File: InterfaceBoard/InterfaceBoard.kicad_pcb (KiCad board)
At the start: 2 copper layers, 100 x 85 mm, 115 parts, among them J1 Conn_ARM_JTAG_SWD_10, J2 USB_B, J3 Keithley_50-Pin_Connector, P1 RB1-125BAG1A, Q1 BC848W, Q2 BC848W, Q3 BC848W, U1 W5500, U2 FT231XS, Y1 25 MHz

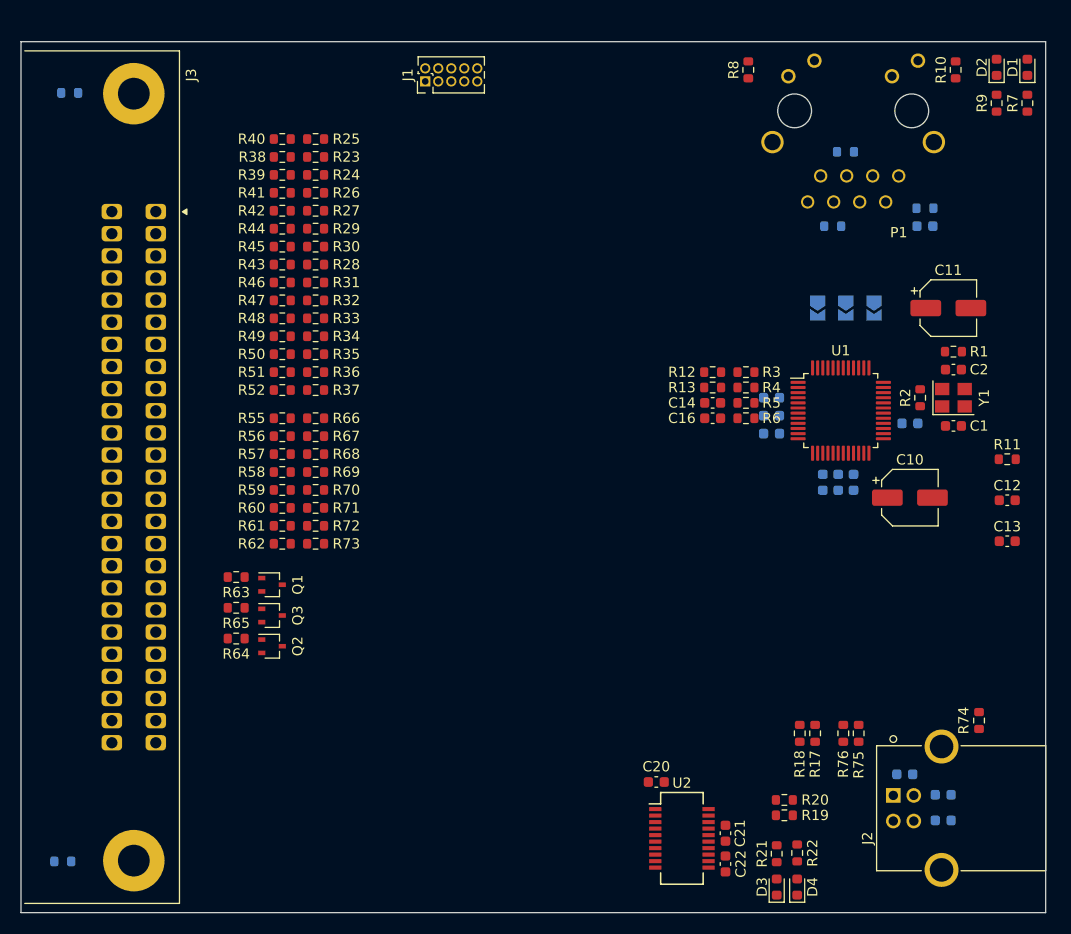
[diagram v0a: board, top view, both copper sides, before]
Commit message: InterfaceBoard: Add RS-232/DE-9
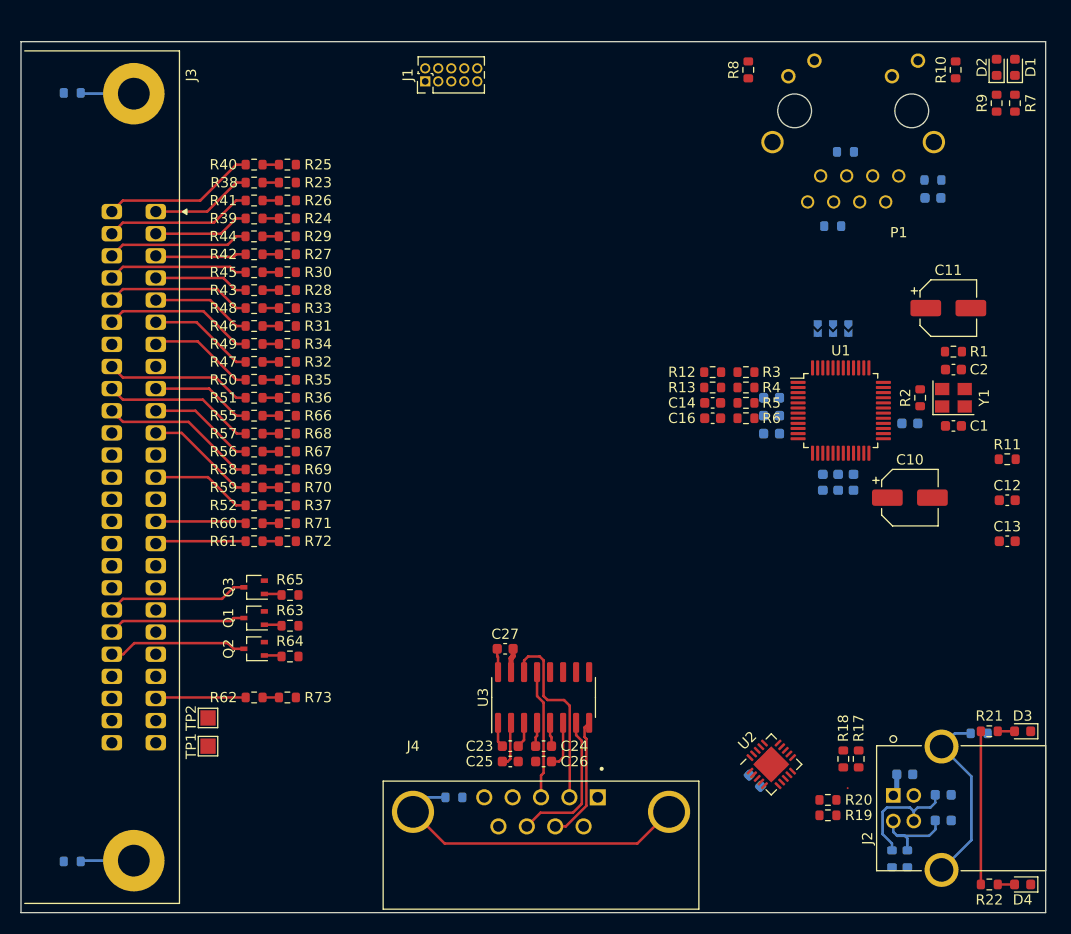
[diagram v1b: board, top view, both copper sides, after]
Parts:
- added C23: 1uF, Capacitor_SMD:C_0603_1608Metric, F.Cu at (87.8, 98.8)
- added C24: 1uF, Capacitor_SMD:C_0603_1608Metric, F.Cu at (91.0, 98.8)
- added C25: 1uF, Capacitor_SMD:C_0603_1608Metric, F.Cu at (87.8, 100.2)
- added C26: 1uF, Capacitor_SMD:C_0603_1608Metric, F.Cu at (91.0, 100.2)
- added C27: 1uF, Capacitor_SMD:C_0603_1608Metric, F.Cu at (87.2, 89.2)
- added J4: DB9_Female_MountingHoles, lib:ASSMANN_A-DF_09_A_KG-T2S, F.Cu at (90.8, 105.2)
- added R77: 0, Resistor_SMD:R_0603_1608Metric, B.Cu at (82.2, 103.8)
- added TP1: Ref Hi, TestPoint:TestPoint_Pad_1.5x1.5mm, F.Cu at (58.2, 98.8)
- added TP2: Ref Lo, TestPoint:TestPoint_Pad_1.5x1.5mm, F.Cu at (58.2, 96.0)
- added U3: MAX232, Package_SO:SOIC-16_3.9x9.9mm_P1.27mm, F.Cu at (91.0, 94.0)
- C20, C21, C22, R74, R75, R76: moved to B.Cu
- JP1, JP2, JP3: footprint Jumper:SolderJumper-2_P1.3mm_Open_TrianglePad1.0x1.5mm -> lib:0603_solder_jumper
- U2: value FT231XS -> FT231XQ; footprint Package_SO:SSOP-20_3.9x8.7mm_P0.635mm -> Package_DFN_QFN:QFN-20-1EP_4x4mm_P0.5mm_EP2.5x2.5mm
- moved D3 28.4 mm to (137.8, 97.3), turned to 180 degrees
- moved R21 23.9 mm to (134.5, 97.3), turned to 180 degrees
- moved D4 22.0 mm to (137.8, 112.2), turned to 180 degrees
- moved R22 19.0 mm to (134.5, 112.2), turned to 180 degrees
- moved R62 15.2 mm to (62.8, 94.0)
- moved R73 15.2 mm to (66.0, 94.0)
- moved R76 13.8 mm to (126.5, 109.8), turned to -90 degrees
- moved R75 12.7 mm to (125.0, 109.8), turned to -90 degrees
- moved R37 11.6 mm to (66.0, 75.2)
- moved R52 11.6 mm to (62.8, 75.2)
- moved U2 11.3 mm to (113.2, 100.5), turned to 45 degrees
- moved C22 10.00 mm to (112.7, 101.1), turned to 135 degrees
- moved C20 9.63 mm to (111.6, 102.1), turned to -45 degrees
- moved C21 8.81 mm to (113.8, 100.0), turned to 135 degrees
- moved R63 7.08 mm to (66.2, 87.0), turned to 180 degrees
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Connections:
- net /50pin/Data_1e0 renamed /Data_1e0
- net /50pin/Data_1e1 renamed /Data_1e1
- net /50pin/Data_1e2 renamed /Data_1e2
- net /50pin/Data_1e3 renamed /Data_1e3
- net /50pin/Data_2e0 renamed /Data_2e0
- net /50pin/Data_2e1 renamed /Data_2e1
- net /50pin/Data_2e2 renamed /Data_2e2
- net /50pin/Data_4e0 renamed /Data_4e0
- net /50pin/Data_4e1 renamed /Data_4e1
- net /50pin/Data_4e2 renamed /Data_4e2
- net /50pin/Data_8e0 renamed /Data_8e0
- net /50pin/Data_8e1 renamed /Data_8e1
- net /50pin/Data_8e2 renamed /Data_8e2
- net /50pin/Hold1 renamed /Hold1
- net /50pin/Hold2 renamed /Hold2
- net /50pin/Overload renamed /Overload
- net /50pin/Polarity renamed /Polarity
- net /50pin/Print_Cmd renamed /Print_Cmd
- net /50pin/Range_1e0 renamed /Range_1e0
- net /50pin/Range_1e1 renamed /Range_1e1
- net /50pin/Range_2e0 renamed /Range_2e0
- net /50pin/Range_4e0 renamed /Range_4e0
- net /50pin/Range_8e0 renamed /Range_8e0
- net /50pin/Sensitivity_1e0 renamed /Sensitivity_1e0
- net /50pin/Sensitivity_2e0 renamed /Sensitivity_2e0
- net /50pin/Trigger renamed /Trigger
- net Net-(C17-Pad1) renamed /USB/USBB_D+
- net Net-(C18-Pad1) renamed /USB/USBB_D-
- C20 pad 1: Net-(C20-Pad1) -> /USB/FTDI_VCC
- D3 pad 1: Net-(D3-Pad1) -> /USB/FTDI_RX_LED
- D4 pad 1: Net-(D4-Pad1) -> /USB/FTDI_TX_LED
- R19 pad 2: Net-(R19-Pad2) -> /USB/FTDI_D+
- R20 pad 2: Net-(R20-Pad2) -> /USB/FTDI_D-
- R21 pad 2: Net-(C20-Pad1) -> /USB/FTDI_VCC
- R22 pad 2: Net-(C20-Pad1) -> /USB/FTDI_VCC
- U2 pad 1: unconnected-(U2-Pad1) -> /USB/USB_UART_RX
- U2 pad 10: Net-(D4-Pad1) -> /USB/FTDI_VCC
- U2 pad 11: Net-(R19-Pad2) -> /USB/FTDI_VCC
- U2 pad 12: Net-(R20-Pad2) -> /USB/V_USB
- U2 pad 13: Net-(C20-Pad1) -> unconnected-(U2-Pad13)
- U2 pad 14: Net-(C20-Pad1) -> /USB/FTDI_RX_LED
- U2 pad 15: /USB/V_USB -> unconnected-(U2-Pad15)
- U2 pad 16: GND -> unconnected-(U2-Pad16)
- U2 pad 17: Net-(D3-Pad1) -> /USB/USB_UART_TX
- U2 pad 19: unconnected-(U2-Pad19) -> /USB/USB_UART_RTS
- U2 pad 2: /USB/USB_UART_RTS -> unconnected-(U2-Pad2)
- U2 pad 20: /USB/USB_UART_TX -> /USB/FTDI_VCC
- U2 pad 3: Net-(C20-Pad1) -> GND
- U2 pad 4: /USB/USB_UART_RX -> unconnected-(U2-Pad4)
- U2 pad 6: GND -> /USB/USB_UART_CTS
- U2 pad 7: unconnected-(U2-Pad7) -> /USB/FTDI_TX_LED
- U2 pad 8: unconnected-(U2-Pad8) -> /USB/FTDI_D+
- U2 pad 9: /USB/USB_UART_CTS -> /USB/FTDI_D-
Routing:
- net Net-(J4-Pad0): track 0.00 -> 31.3 mm
- net Net-(J4-Pad2): track 0.00 -> 18.7 mm
- net Net-(J2-PadSH1): track 0.00 -> 17.8 mm
- net Net-(J3-Pad35): track 0.00 -> 15.4 mm
- net /USB/FTDI_VCC: track 0.00 -> 15.0 mm
- net Net-(J3-Pad26): track 0.00 -> 15.0 mm
- net Net-(J3-Pad34): track 0.00 -> 14.9 mm
- net Net-(J3-Pad31): track 0.00 -> 14.8 mm
- net Net-(J4-Pad8): track 0.00 -> 14.4 mm
- net Net-(J3-Pad27): track 0.00 -> 14.4 mm
- net Net-(J3-Pad33): track 0.00 -> 14.3 mm
- net Net-(J3-Pad30): track 0.00 -> 14.3 mm
- net Net-(J3-Pad28): track 0.00 -> 13.8 mm
- net Net-(J3-Pad44): track 0.00 -> 13.8 mm
- net Net-(J3-Pad29): track 0.00 -> 13.7 mm
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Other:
- copper layers 2 -> 4

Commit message: InterfaceBoard: Add STM32G0B1RET
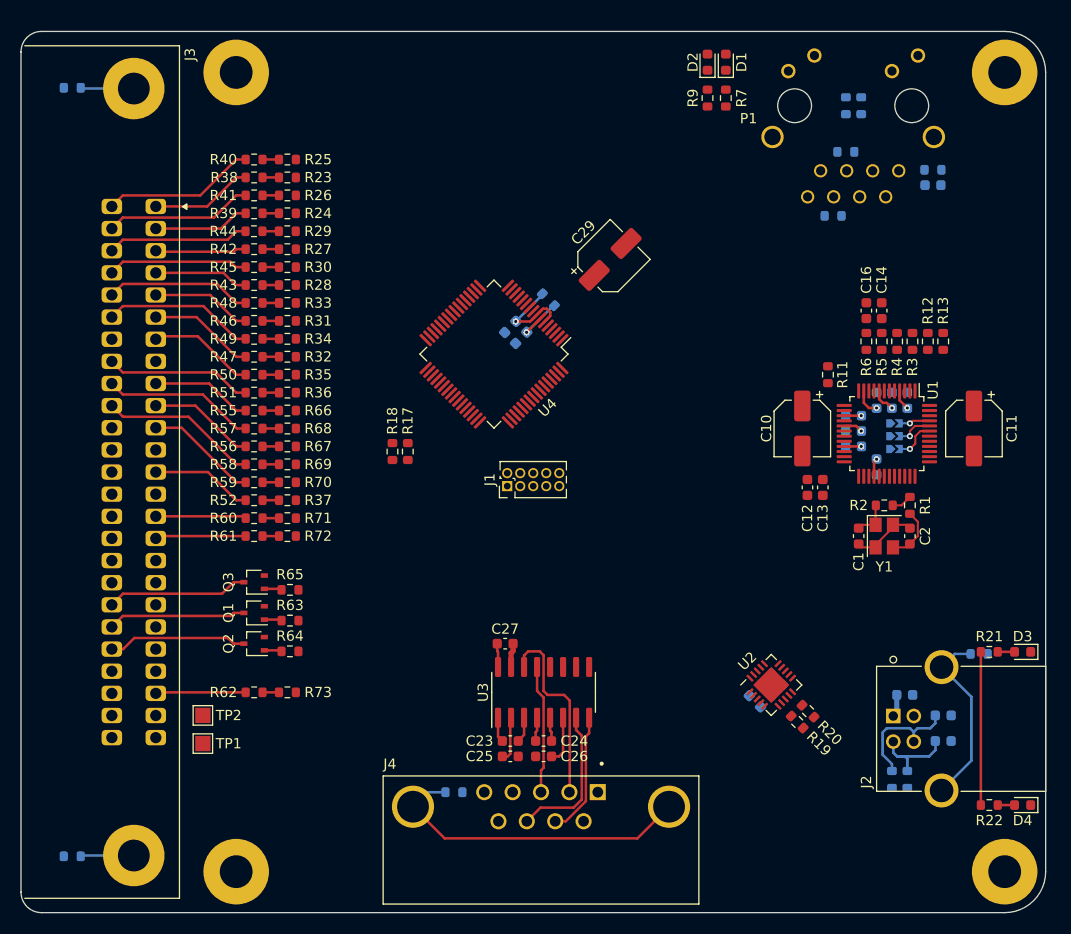
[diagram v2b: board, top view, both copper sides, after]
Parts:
- added C28: 100nF, Capacitor_SMD:C_0603_1608Metric, B.Cu at (87.8, 57.8)
- added C29: 4.7uF, Capacitor_SMD:CP_Elec_5x5.9, F.Cu at (97.5, 51.2)
- added C30: 100nF, Capacitor_SMD:C_0603_1608Metric, B.Cu at (88.8, 58.9)
- added H1: MountingHole_Pad, MountingHole:MountingHole_3.2mm_M3_Pad, F.Cu at (136.0, 111.0)
- added H2: MountingHole_Pad, MountingHole:MountingHole_3.2mm_M3_Pad, F.Cu at (136.0, 33.0)
- added H3: MountingHole_Pad, MountingHole:MountingHole_3.2mm_M3_Pad, F.Cu at (61.0, 111.0)
- added H4: MountingHole_Pad, MountingHole:MountingHole_3.2mm_M3_Pad, F.Cu at (61.0, 33.0)
- added R78: 0, Resistor_SMD:R_0603_1608Metric, B.Cu at (91.5, 55.2)
- added U4: STM32G0B1RET, Package_QFP:LQFP-64_10x10mm_P0.5mm, F.Cu at (86.2, 60.5)
- R10, R8: moved to B.Cu
- moved R17 53.3 mm to (77.8, 70.0)
- moved R18 53.3 mm to (76.2, 70.0)
- moved J1 40.3 mm to (87.5, 73.4)
- moved D2 28.2 mm to (107.0, 32.0)
- moved R9 28.2 mm to (107.0, 35.5)
- moved D1 28.2 mm to (108.8, 32.0)
- moved R7 28.2 mm to (108.8, 35.5)
- moved R13 22.9 mm to (130.0, 59.2), turned to 90 degrees
- moved R12 21.2 mm to (128.5, 59.2), turned to 90 degrees
- moved C12 19.5 mm to (116.8, 73.5), turned to -90 degrees
- moved R11 19.3 mm to (118.8, 62.5), turned to -90 degrees
- moved C14 18.8 mm to (124.0, 56.2), turned to 90 degrees
- moved C13 18.8 mm to (118.2, 73.5), turned to -90 degrees
- moved C16 18.3 mm to (122.5, 56.2), turned to 90 degrees
- moved C2 16.8 mm to (126.8, 78.2), turned to -90 degrees
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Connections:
- net Net-(C14-Pad2) renamed /Ethernet Interface/ETH_PORT_RX-
- net Net-(C15-Pad2) renamed /Ethernet Interface/ETH_PORT_CT
- net Net-(C16-Pad2) renamed /Ethernet Interface/ETH_PORT_RX+
- net Net-(JP1-Pad2) renamed /Ethernet Interface/PMODE0
- net Net-(JP2-Pad2) renamed /Ethernet Interface/PMODE1
- net Net-(JP3-Pad2) renamed /Ethernet Interface/PMODE2
- net Net-(P1-PadL2) renamed /Ethernet Interface/ETH_LED_LINK
- net Net-(P1-PadL4) renamed /Ethernet Interface/ETH_LED_ACT
- net Net-(P1-PadR1) renamed /Ethernet Interface/ETH_PORT_TX+
- net Net-(P1-PadR2) renamed /Ethernet Interface/ETH_PORT_TX-
- J1 pad 10: unconnected-(J1-Pad10) -> /MCU/NRST
- J1 pad 2: unconnected-(J1-Pad2) -> /MCU/SWD_SWDIO
- J1 pad 3: Net-(J1-Pad3) -> GND
- J1 pad 4: unconnected-(J1-Pad4) -> /MCU/SWD_SWCLK
- J1 pad 5: Net-(J1-Pad3) -> GND
- J1 pad 9: unconnected-(J1-Pad9) -> GND
- R17 pad 2: /USB/USB_DP -> /MCU/USB_D+
- R18 pad 2: /USB/USB_DM -> /MCU/USB_D-
- U2 pad 1: /USB/USB_UART_RX -> /MCU/USB_UART_RX
- U2 pad 17: /USB/USB_UART_TX -> /MCU/USB_UART_TX
- U2 pad 19: /USB/USB_UART_RTS -> /MCU/USB_UART_CTS
- U2 pad 6: /USB/USB_UART_CTS -> /MCU/USB_UART_RTS
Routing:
- net +3V3: track 0.00 -> 23.0 mm, vias 0 -> 8
- net GND: track 2.36 -> 8.83 mm
- net /MCU/VREF+: track 0.00 -> 5.68 mm, vias 0 -> 1
- net Net-(C2-Pad2): track 0.00 -> 5.38 mm
- net /Ethernet Interface/PMODE2: track 0.00 -> 3.96 mm, vias 0 -> 1
- net Net-(C1-Pad2): track 0.00 -> 3.69 mm
- net /Ethernet Interface/PMODE1: track 0.00 -> 3.52 mm, vias 0 -> 1
- net /Ethernet Interface/PMODE0: track 0.00 -> 2.92 mm, vias 0 -> 1
- net Net-(R1-Pad2): track 0.00 -> 2.02 mm
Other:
- board size 100 x 85 mm -> 100 x 86 mm

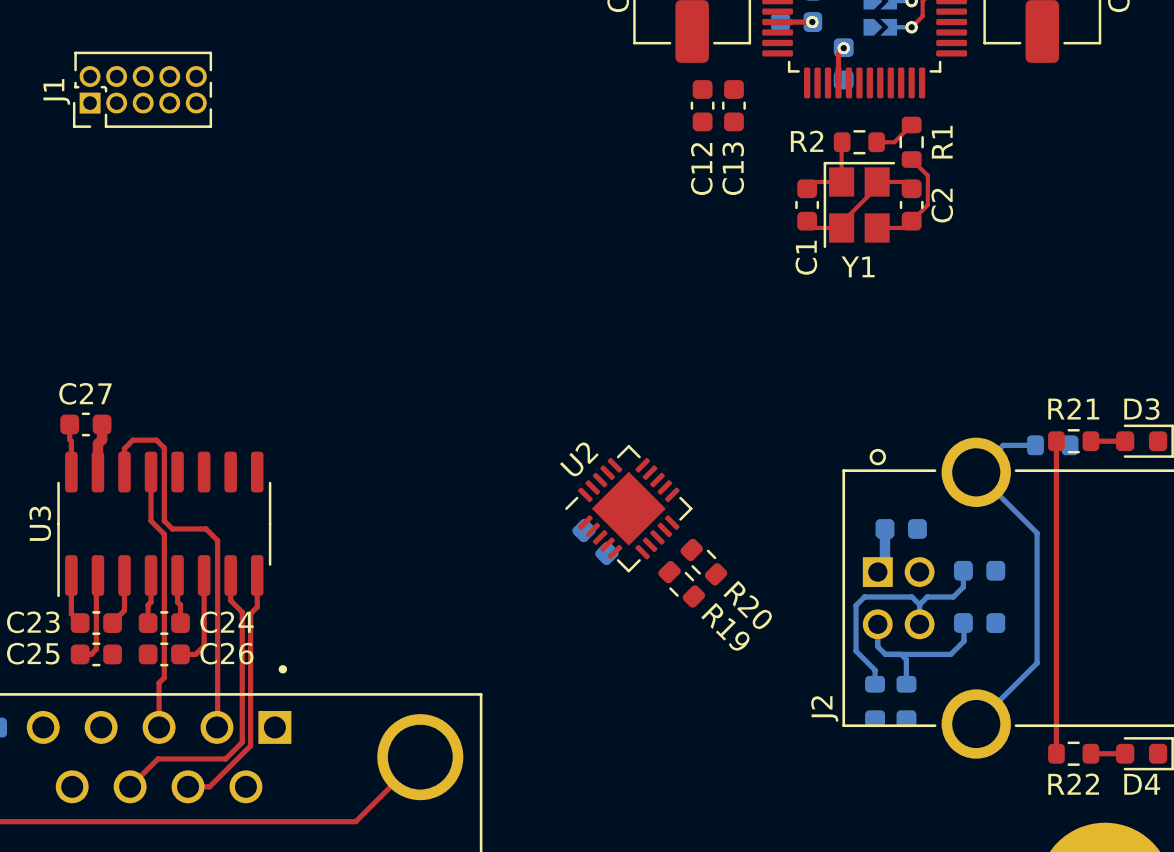
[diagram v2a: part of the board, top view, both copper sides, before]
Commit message: InterfaceBoard: Make library paths relative
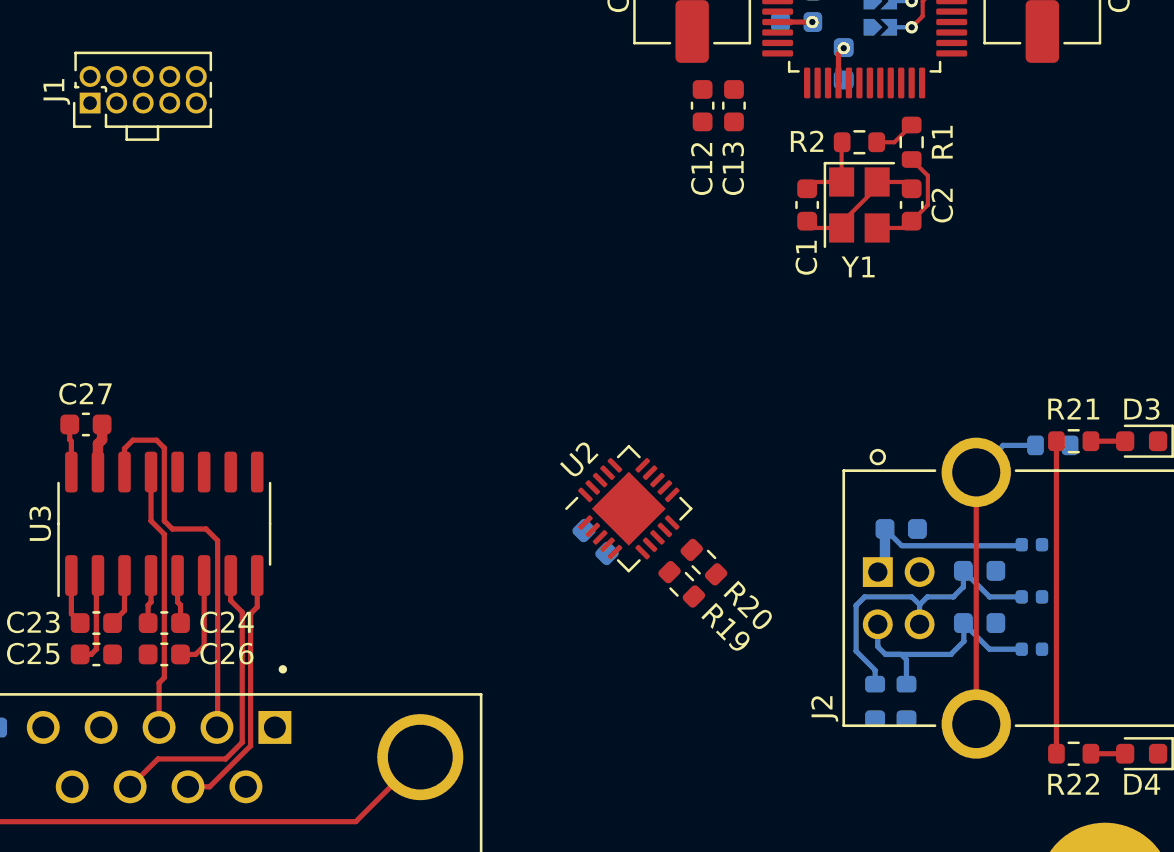
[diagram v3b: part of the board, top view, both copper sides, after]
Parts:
- added D5: PE1605M1Q, Diode_SMD:D_0402_1005Metric, B.Cu at (132.5, 94.5)
- added D6: PE1605M1Q, Diode_SMD:D_0402_1005Metric, B.Cu at (132.5, 99.5)
- added D7: PE1605M1Q, Diode_SMD:D_0402_1005Metric, B.Cu at (132.5, 97.0)
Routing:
- net /USB/V_USB: track 2.20 -> 9.09 mm
- net /USB/USBB_D-: track 9.09 -> 12.4 mm
- net /USB/USBB_D+: track 11.7 -> 15.0 mm
- net Net-(J2-PadSH1): track 17.8 -> 15.4 mm
